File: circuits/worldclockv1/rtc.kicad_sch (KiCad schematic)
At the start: 9 parts, among them U2 DS3232M

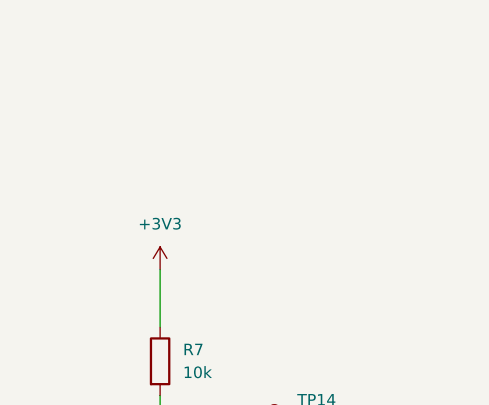
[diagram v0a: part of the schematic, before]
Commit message: World Clock PCB completed
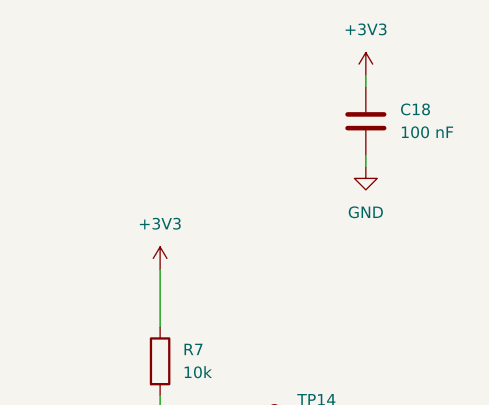
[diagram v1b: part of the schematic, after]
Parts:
- added C18: 100 nF, Capacitor_SMD:C_1206_3216Metric_Pad1.33x1.80mm_HandSolder, symbol Device:C
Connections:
- net +3V3: now also C18.1
- net GND: now also C18.2
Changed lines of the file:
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@@
+	(wire
+		(pts
+			(xy 176.53 31.75) (xy 176.53 33.02)
+		)
+		(stroke
+			(width 0)
+			(type default)
+		)
+	)
 	(wire
 		(pts
@@
 		(pts
 			(xy 44.45 72.39) (xy 68.58 72.39)
+		)
+		(stroke
+			(width 0)
+			(type default)
+		)
+	)
+	(wire
+		(pts
+			(xy 176.53 40.64) (xy 176.53 41.91)
 		)
 		(stroke
@@
 	)
 	(symbol
+		(lib_id "Device:C")
+		(at 176.53 36.83 0)
+		(unit 1)
+		(exclude_from_sim no)
+		(in_bom yes)
+		(on_board yes)
+		(dnp no)
+		(fields_autoplaced yes)
+		(property "Reference" "C18"
+			(at 180.34 35.5599 0)
+			(effects
+				(font
+					(size 1.27 1.27)
+				)
+				(justify left)
+			)
+		)
+		(property "Value" "100 nF"
+			(at 180.34 38.0999 0)
+			(effects
+				(font
+					(size 1.27 1.27)
+				)
+				(justify left)
+			)
+		)
+		(property "Footprint" "Capacitor_SMD:C_1206_3216Metric_Pad1.33x1.80mm_HandSolder"
+			(at 177.4952 40.64 0)
+			(effects
+				(font
+					(size 1.27 1.27)
+				)
+				(hide yes)
+			)
+		)
+		(property "Datasheet" "~"
+			(at 176.53 36.83 0)
+			(effects
+				(font
+					(size 1.27 1.27)
+				)
+				(hide yes)
+			)
+		)
+		(property "Description" "Unpolarized capacitor"
+			(at 176.53 36.83 0)
+			(effects
+				(font
+					(size 1.27 1.27)
+				)
+				(hide yes)
+			)
+		)
+		(pin "1"
+		)
+		(pin "2"
+		)
+		(instances
+			(project "worldclockv1"
+				(path "/535d2189-216d-4902-a433-29ee220a5002/8ddc645a-6419-406d-9ff8-2545978192c7"
+					(reference "C18")
+					(unit 1)
+				)
+			)
+		)
+	)
+	(symbol
 		(lib_id "Device:R")
 		(at 153.67 63.5 0)
@@
 	)
 	(symbol
+		(lib_id "power:+3V3")
+		(at 176.53 31.75 0)
+		(unit 1)
+		(exclude_from_sim no)
+		(in_bom yes)
+		(on_board yes)
+		(dnp no)
+		(fields_autoplaced yes)
+		(property "Reference" "#PWR048"
+			(at 176.53 35.56 0)
+			(effects
+				(font
+					(size 1.27 1.27)
+				)
+				(hide yes)
+			)
+		)
+		(property "Value" "+3V3"
+			(at 176.53 26.67 0)
+			(effects
+				(font
+					(size 1.27 1.27)
+				)
+			)
+		)
+		(property "Footprint" ""
+			(at 176.53 31.75 0)
+			(effects
+				(font
+					(size 1.27 1.27)
+				)
+				(hide yes)
+			)
+		)
+		(property "Datasheet" ""
+			(at 176.53 31.75 0)
+			(effects
+				(font
+					(size 1.27 1.27)
+				)
+				(hide yes)
+			)
+		)
+		(property "Description" "Power symbol creates a global label with name \"+3V3\""
+			(at 176.53 31.75 0)
+			(effects
+				(font
+					(size 1.27 1.27)
+				)
+				(hide yes)
+			)
+		)
+		(pin "1"
+		)
+		(instances
+			(project "worldclockv1"
+				(path "/535d2189-216d-4902-a433-29ee220a5002/8ddc645a-6419-406d-9ff8-2545978192c7"
+					(reference "#PWR048")
+					(unit 1)
+				)
+			)
+		)
+	)
+	(symbol
 		(lib_id "Connector:TestPoint")
 		(at 68.58 64.77 0)
@@
 					(unit 1)
 				)
+			)
+		)
+	)
+	(symbol
+		(lib_id "power:GND")
+		(at 176.53 41.91 0)
+		(unit 1)
+		(exclude_from_sim no)
+		(in_bom yes)
+		(on_board yes)
+		(dnp no)
+		(fields_autoplaced yes)
+		(property "Reference" "#PWR049"
+			(at 176.53 48.26 0)
+			(effects
+				(font
+					(size 1.27 1.27)
+				)
+				(hide yes)
+			)
+		)
+		(property "Value" "GND"
+			(at 176.53 46.99 0)
+			(effects
+				(font
+					(size 1.27 1.27)
+				)
+			)
+		)
+		(property "Footprint" ""
+			(at 176.53 41.91 0)
+			(effects
+				(font
+					(size 1.27 1.27)
+				)
+				(hide yes)
+			)
+		)
+		(property "Datasheet" ""
+			(at 176.53 41.91 0)
+			(effects
+				(font
+					(size 1.27 1.27)
+				)
+				(hide yes)
+			)
+		)
+		(property "Description" "Power symbol creates a global label with name \"GND\" , ground"
+			(at 176.53 41.91 0)
+			(effects
+				(font
+					(size 1.27 1.27)
+				)
+				(hide yes)
+			)
+		)
+		(pin "1"
+		)
+		(instances
+			(project "worldclockv1"
+				(path "/535d2189-216d-4902-a433-29ee220a5002/8ddc645a-6419-406d-9ff8-2545978192c7"
+					(reference "#PWR049")
+					(unit 1)
+				)
